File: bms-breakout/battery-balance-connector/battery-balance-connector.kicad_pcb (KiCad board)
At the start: 2 copper layers, 61 x 38.1 mm, 10 parts, among them J1 Conn_01x04, J10 Conn_01x01, J2 Conn_01x04, J3 Conn_01x01, J4 Conn_01x01, J5 Conn_01x01, J6 Conn_01x01, J7 Conn_01x01, J8 Conn_01x01, J9 Conn_01x01

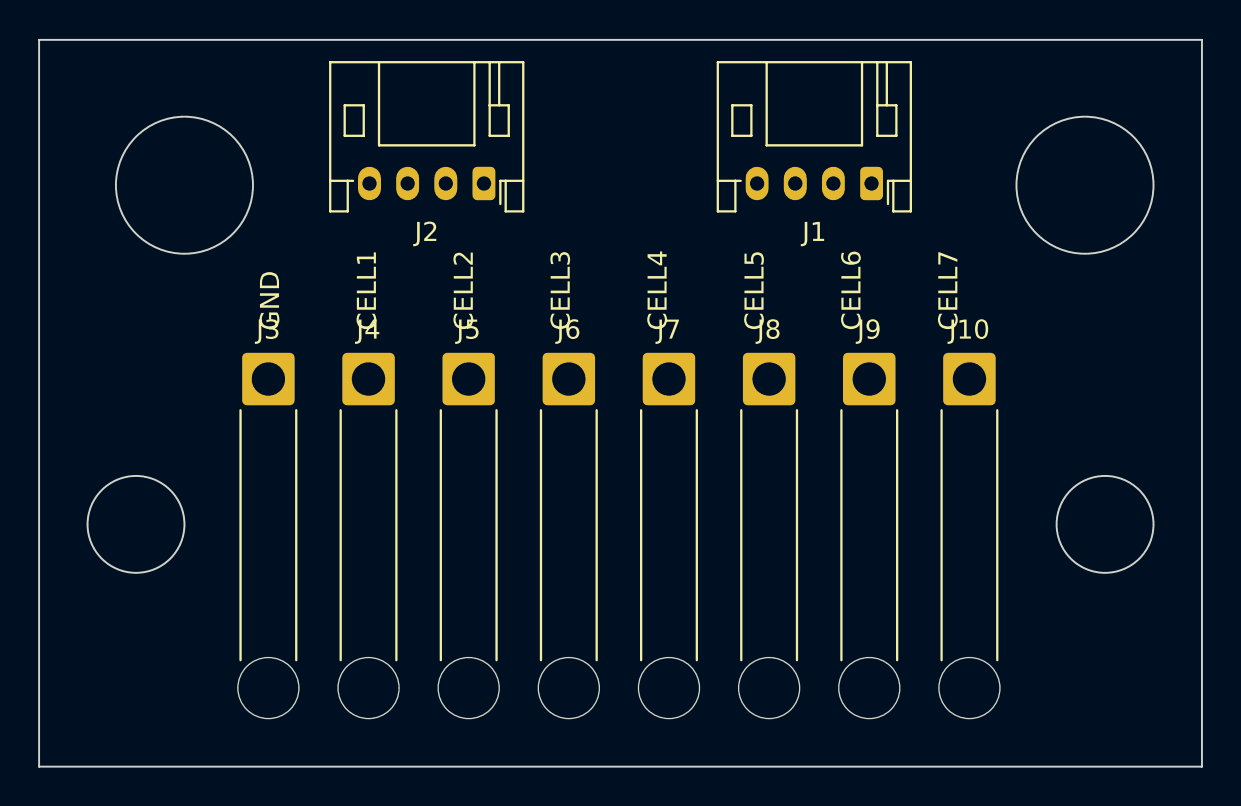
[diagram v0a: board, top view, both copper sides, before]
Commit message: V1.0.0 of battery balance connector
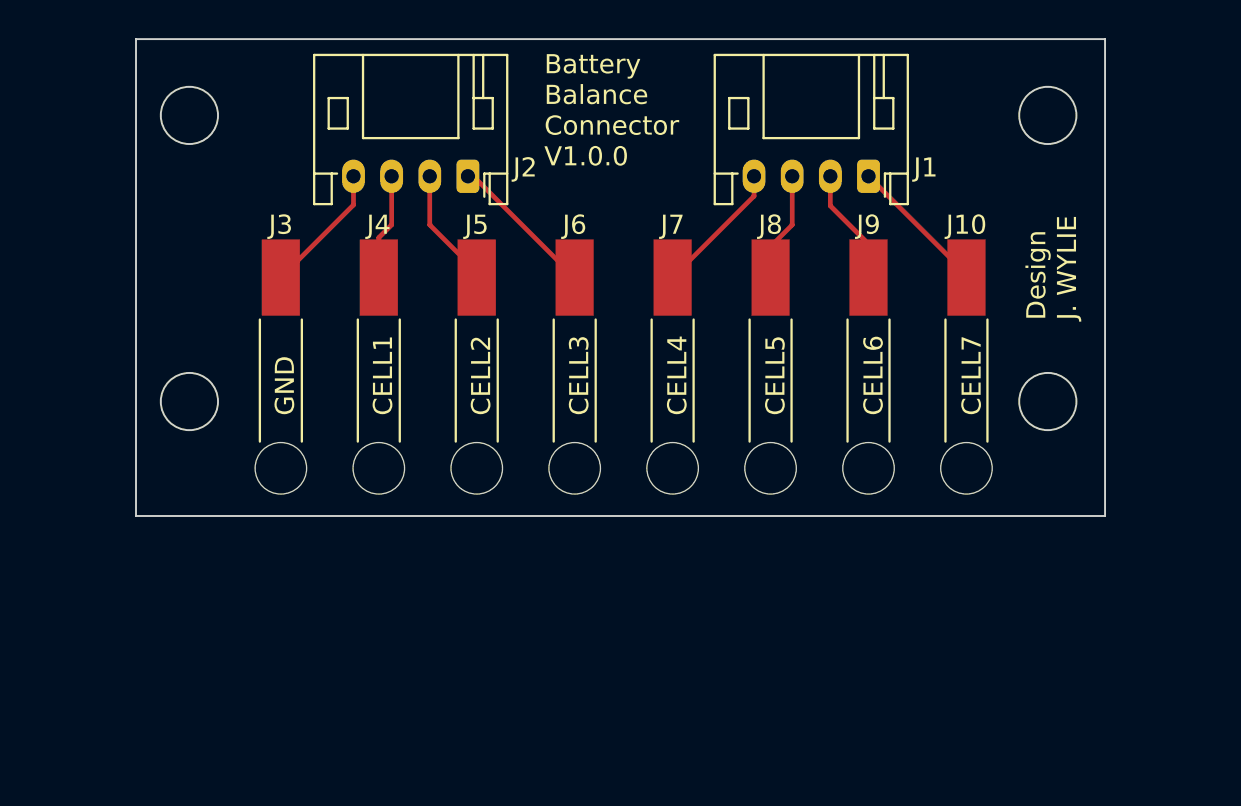
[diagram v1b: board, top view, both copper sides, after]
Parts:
- J10, J3, J4, J5, J6, J7, J8, J9: footprint Connector_Wire:SolderWire-1sqmm_1x01_D1.4mm_OD2.7mm_Relief -> Connector_Wire:SolderWirePad_1x01_SMD_2x4mm_2.7mmRelief
- moved J3 5.36 mm to (83.8, 78.5)
- moved J4 5.35 mm to (88.9, 78.5)
- moved J5 5.34 mm to (94.1, 78.5)
- moved J6 5.33 mm to (99.2, 78.5)
- moved J7 5.32 mm to (104.3, 78.5)
- moved J10 5.32 mm to (119.7, 78.5)
- moved J8 5.32 mm to (109.5, 78.5)
- moved J9 5.32 mm to (114.6, 78.5)
- moved J2 0.92 mm to (93.6, 73.2)
- moved J1 0.41 mm to (114.6, 73.2)
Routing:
- net /CELL3: track 0.00 -> 7.80 mm
- net /CELL7: track 0.00 -> 7.44 mm
- net /CELL4: track 0.00 -> 7.08 mm
- net GND: track 0.00 -> 6.89 mm
- net /CELL2: track 0.00 -> 6.33 mm
- net /CELL6: track 0.00 -> 6.14 mm
- net /CELL5: track 0.00 -> 5.78 mm
- net /CELL1: track 0.00 -> 5.59 mm
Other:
- board size 61 x 38.1 mm -> 50.8 x 25 mm
- board text added: "Battery Balance Connector V1.0.0"
- board text added: "Design J. WYLIE"

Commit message: V1.0.1 - using vertical mounting and tweaked dimensions
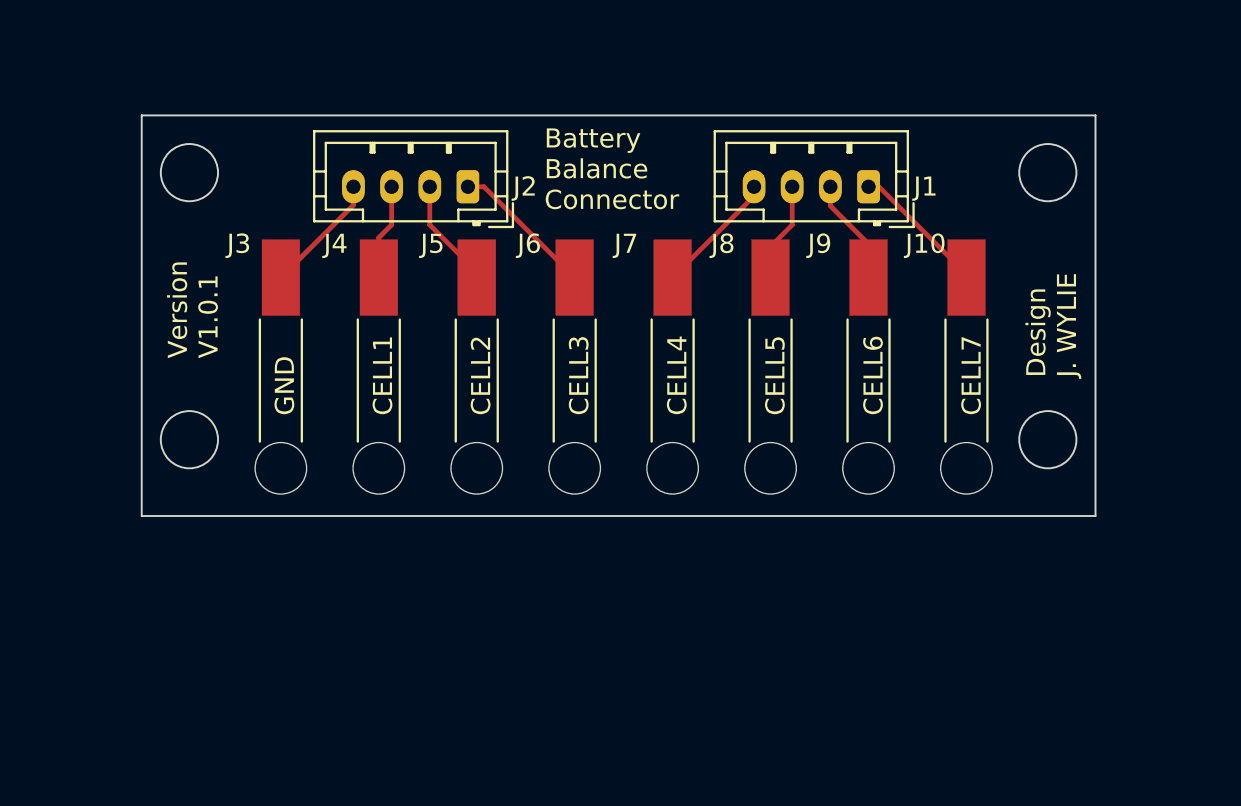
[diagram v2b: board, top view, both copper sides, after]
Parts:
- J1, J2: footprint Connector_JST:JST_PH_S4B-PH-K_1x04_P2.00mm_Horizontal -> Connector_JST:JST_PH_B4B-PH-K_1x04_P2.00mm_Vertical
- moved J1 0.55 mm to (114.6, 73.7)
- moved J2 0.55 mm to (93.6, 73.7)
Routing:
- net GND: track 6.89 -> 6.34 mm
- net /CELL6: track 6.14 -> 5.59 mm
- net /CELL5: track 5.78 -> 5.23 mm
- net /CELL4: track 7.08 -> 6.53 mm
- net /CELL2: track 6.33 -> 5.78 mm
- net /CELL1: track 5.59 -> 5.04 mm
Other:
- board size 50.8 x 25 mm -> 50 x 21 mm
- board text added: "Battery Balance Connector"
- board text added: "Version V1.0.1"
- board text removed: "Battery Balance Connector V1.0.0"

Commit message: gerbers for V1.0.1 of battery balance leads connector
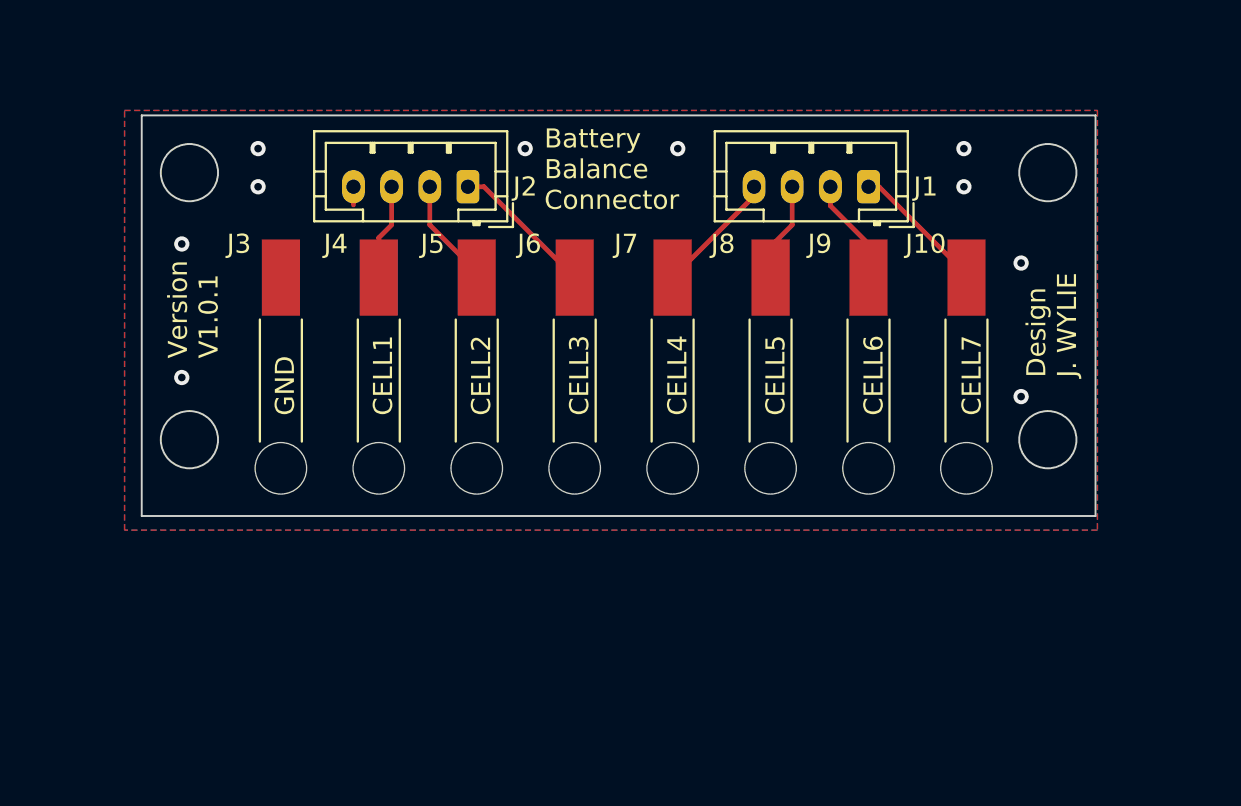
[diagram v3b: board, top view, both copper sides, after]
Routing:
- net GND: track 6.34 -> 0.95 mm, vias 0 -> 10
- added copper zone on B.Cu, net GND
- added copper zone on F.Cu, net GND
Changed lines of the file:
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@@
       (plot_on_all_layers_selection 0x0000000_00000000)
       (disableapertmacros false)
-      (usegerberextensions false)
-      (usegerberattributes true)
-      (usegerberadvancedattributes true)
-      (creategerberjobfile true)
+      (usegerberextensions true)
+      (usegerberattributes false)
+      (usegerberadvancedattributes false)
+      (creategerberjobfile false)
       (dashed_line_dash_ratio 12.000000)
       (dashed_line_gap_ratio 3.000000)
@@
       (psa4output false)
       (plotreference true)
-      (plotvalue true)
+      (plotvalue false)
       (plotinvisibletext false)
       (sketchpadsonfab false)
-      (subtractmaskfromsilk false)
+      (subtractmaskfromsilk true)
       (outputformat 1)
       (mirror false)
-      (drillshape 1)
+      (drillshape 0)
       (scaleselection 1)
-      (outputdirectory "")
+      (outputdirectory "production-v1.0.1/")
     )
   )
@@
     (fp_line (start 7.95 2.8) (end 7.95 -1.7)
       (stroke (width 0.1) (type solid)) (layer "F.Fab"))
-    (pad "1" thru_hole roundrect (at 0 0 180) (size 1.2 1.75) (drill 0.75) (layers "*.Cu" "*.Mask") (roundrect_rratio 0.208333)
+    (pad "1" thru_hole roundrect (at 0 0 180) (size 1.2 1.75) (drill 0.75) (layers "*.Cu" "*.Mask") (roundrect_rratio 0.2083333333)
       (net 8 "/CELL3") (pinfunction "Pin_1") (pintype "passive"))
     (pad "2" thru_hole oval (at 2 0 180) (size 1.2 1.75) (drill 0.75) (layers "*.Cu" "*.Mask")
@@
     (fp_line (start 7.95 2.8) (end 7.95 -1.7)
       (stroke (width 0.1) (type solid)) (layer "F.Fab"))
-    (pad "1" thru_hole roundrect (at 0 0 180) (size 1.2 1.75) (drill 0.75) (layers "*.Cu" "*.Mask") (roundrect_rratio 0.208333)
+    (pad "1" thru_hole roundrect (at 0 0 180) (size 1.2 1.75) (drill 0.75) (layers "*.Cu" "*.Mask") (roundrect_rratio 0.2083333333)
       (net 1 "/CELL7") (pinfunction "Pin_1") (pintype "passive"))
     (pad "2" thru_hole oval (at 2 0 180) (size 1.2 1.75) (drill 0.75) (layers "*.Cu" "*.Mask")
@@
     )
   )
+  (gr_circle (center 125.6 66.74) (end 125.6 66.74)
+    (stroke (width 0.2) (type default)) (fill none) (layer "F.Cu"))
   (gr_circle (center 124 73) (end 125.5 73)
     (stroke (width 0.1) (type default)) (fill none) (layer "Edge.Cuts"))
@@
   (segment (start 104.33125 78.5) (end 108.6 74.23125) (width 0.25) (layer "F.Cu") (net 4))
   (segment (start 87.6 74.69375) (end 87.6 73.74) (width 0.25) (layer "F.Cu") (net 5))
-  (segment (start 83.79375 78.5) (end 87.6 74.69375) (width 0.25) (layer "F.Cu") (net 5))
+  (via (at 119.6 73.74) (size 0.8) (drill 0.4) (layers "F.Cu" "B.Cu") (free) (net 5))
+  (via (at 96.6 71.74) (size 0.8) (drill 0.4) (layers "F.Cu" "B.Cu") (free) (net 5))
+  (via (at 122.6 77.74) (size 0.8) (drill 0.4) (layers "F.Cu" "B.Cu") (free) (net 5))
+  (via (at 78.6 83.74) (size 0.8) (drill 0.4) (layers "F.Cu" "B.Cu") (free) (net 5))
+  (via (at 122.6 84.74) (size 0.8) (drill 0.4) (layers "F.Cu" "B.Cu") (free) (net 5))
+  (via (at 119.6 71.74) (size 0.8) (drill 0.4) (layers "F.Cu" "B.Cu") (free) (net 5))
+  (via (at 82.6 73.74) (size 0.8) (drill 0.4) (layers "F.Cu" "B.Cu") (free) (net 5))
+  (via (at 104.6 71.74) (size 0.8) (drill 0.4) (layers "F.Cu" "B.Cu") (free) (net 5))
+  (via (at 82.6 71.74) (size 0.8) (drill 0.4) (layers "F.Cu" "B.Cu") (free) (net 5))
+  (via (at 78.6 76.74) (size 0.8) (drill 0.4) (layers "F.Cu" "B.Cu") (free) (net 5))
   (segment (start 88.928125 76.411875) (end 89.6 75.74) (width 0.25) (layer "F.Cu") (net 6))
   (segment (start 89.6 75.74) (end 89.6 73.74) (width 0.25) (layer "F.Cu") (net 6))
@@
   (segment (start 99.196875 78.5) (end 94.436875 73.74) (width 0.25) (layer "F.Cu") (net 8))
   (segment (start 94.436875 73.74) (end 93.6 73.74) (width 0.25) (layer "F.Cu") (net 8))
+  (zone (net 5) (net_name "GND") (layers "F&B.Cu") (hatch edge 0.5)
+    (connect_pads (clearance 0.5))
+    (min_thickness 0.25) (filled_areas_thickness no)
+    (fill yes (thermal_gap 0.5) (thermal_bridge_width 0.5))
+    (polygon
+      (pts
+        (xy 75.6 69.74)
+        (xy 126.6 69.74)
+        (xy 126.6 91.74)
+        (xy 75.6 91.74)
+      )
+    )
+  )
 )
